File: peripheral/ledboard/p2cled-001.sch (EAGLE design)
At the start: 5 parts, among them J3 DISP, J4 PWR

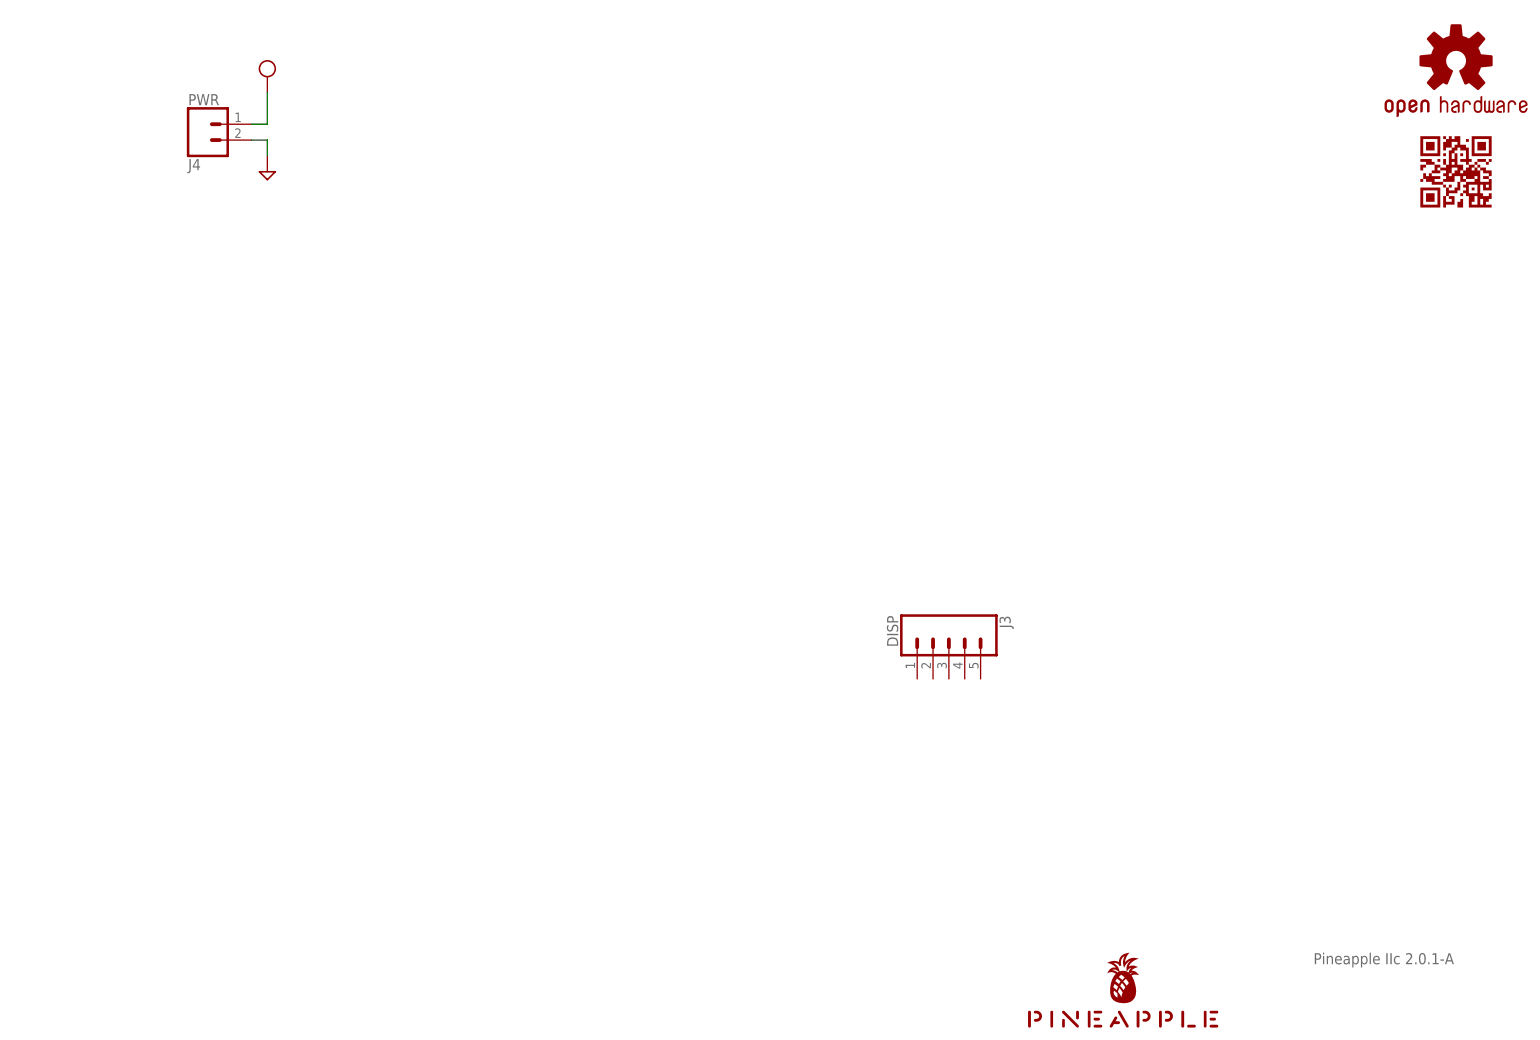
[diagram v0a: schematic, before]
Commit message: Added LED board design.
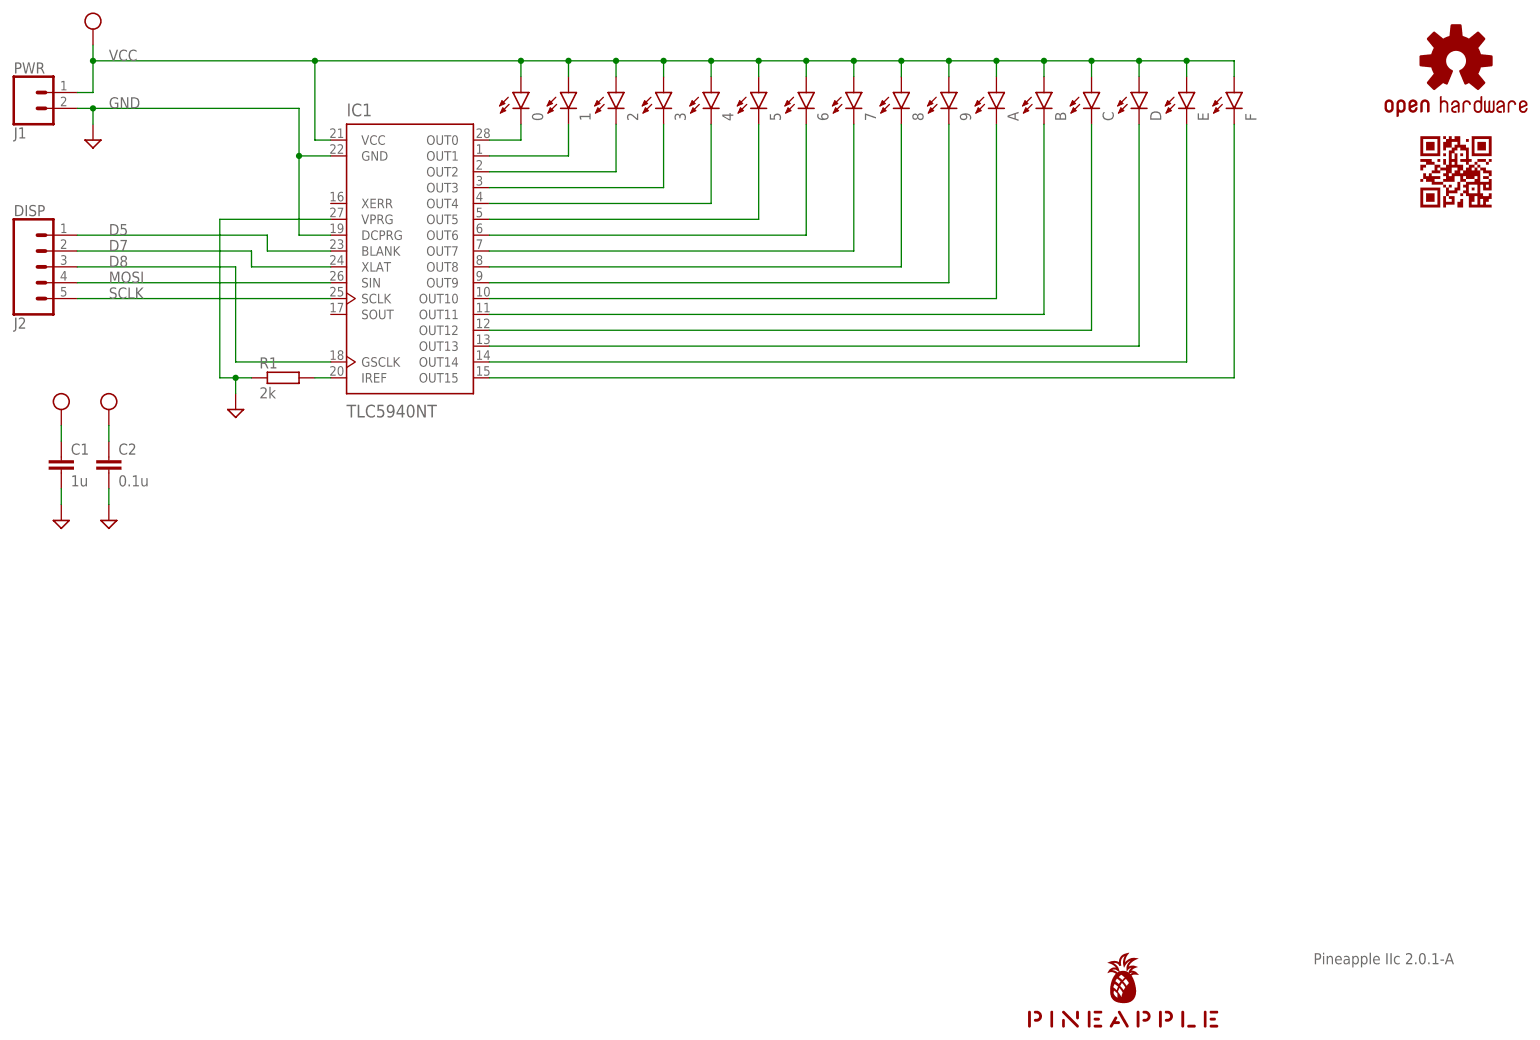
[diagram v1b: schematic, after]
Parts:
- removed J3: DISP, SparkFun-Connectors:CONN_05JST
- removed J4: PWR, SparkFun-Connectors:CONN_02JST-PTH-2
- added 0, 1, 2, 3, 4, 5, 6, 7, 8, 9, A, B, C, D, E, F: (no value), led:LEDB152
- added C1: 1u, resistor:C-EU025-024X044
- added C2: 0.1u, resistor:C-EU025-024X044
- added IC1: TLC5940NT, tlc5940:TLC5940NT
- added J1: PWR, SparkFun-Connectors:CONN_02JST-PTH-2
- added J2: DISP, SparkFun-Connectors:CONN_05JST
- added R1: 2k, resistor:R-EU_0204/5
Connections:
- new net D5: IC1.BLANK, J2.1
- new net D7: IC1.XLAT, J2.2
- new net D8: IC1.GSCLK, J2.3
- new net MOSI: IC1.SIN, J2.4
- new net N$1: 0.C, IC1.OUT0
- new net N$10: 9.C, IC1.OUT9
- new net N$11: A.C, IC1.OUT10
- new net N$12: B.C, IC1.OUT11
- new net N$13: C.C, IC1.OUT12
- new net N$14: D.C, IC1.OUT13
- new net N$15: E.C, IC1.OUT14
- new net N$16: F.C, IC1.OUT15
- new net N$17: IC1.IREF, R1.2
- new net N$2: 1.C, IC1.OUT1
- new net N$3: 2.C, IC1.OUT2
- new net N$4: 3.C, IC1.OUT3
- new net N$5: 4.C, IC1.OUT4
- new net N$6: 5.C, IC1.OUT5
- new net N$7: 6.C, IC1.OUT6
- new net N$8: 7.C, IC1.OUT7
- new net N$9: 8.C, IC1.OUT8
- new net SCLK: IC1.SCLK, J2.5
- net GND: now also C1.2, C2.2, IC1.DCPRG, IC1.GND, IC1.VPRG, J1.2, R1.1; no longer J4.2
- net VCC: now also 0.A, 1.A, 2.A, 3.A, 4.A, 5.A, 6.A, 7.A, 8.A, 9.A, A.A, B.A, C.A, C1.1, C2.1, D.A, E.A, F.A, IC1.VCC, J1.1; no longer J4.1

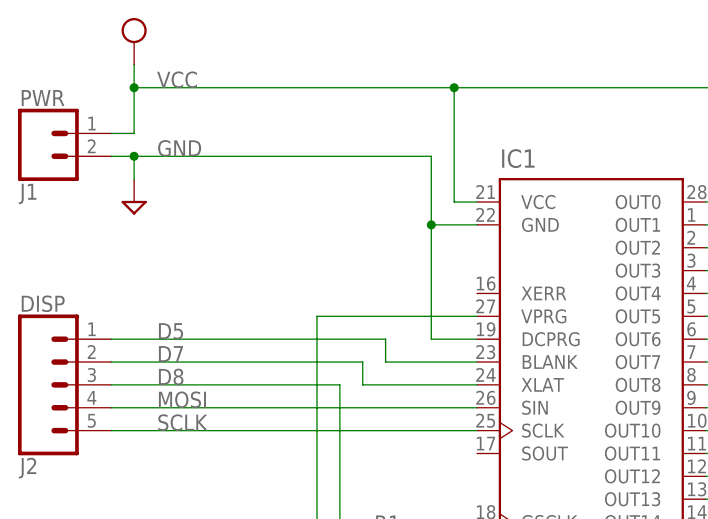
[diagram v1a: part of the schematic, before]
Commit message: Fixed connection of LED board.
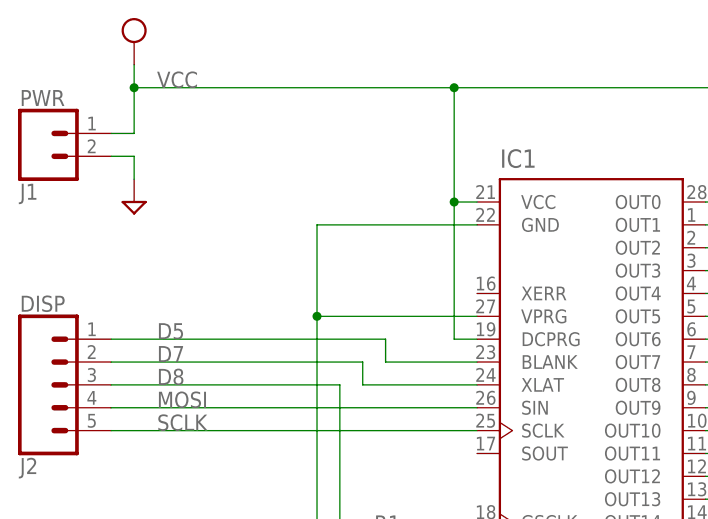
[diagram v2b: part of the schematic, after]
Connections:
- net GND: no longer IC1.DCPRG
- net VCC: now also IC1.DCPRG
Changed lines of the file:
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@@
 <net name="GND" class="1">
 <segment>
+<pinref part="SUPPLY12" gate="GND" pin="GND"/>
 <pinref part="J1" gate="G$1" pin="2"/>
 <wire x1="20.32" y1="157.48" x2="22.86" y2="157.48" width="0.1524" layer="91"/>
-<pinref part="SUPPLY12" gate="GND" pin="GND"/>
 <wire x1="22.86" y1="157.48" x2="22.86" y2="154.94" width="0.1524" layer="91"/>
-<pinref part="IC1" gate="G$1" pin="GND"/>
-<wire x1="60.96" y1="149.86" x2="55.88" y2="149.86" width="0.1524" layer="91"/>
-<wire x1="55.88" y1="149.86" x2="55.88" y2="157.48" width="0.1524" layer="91"/>
-<wire x1="55.88" y1="157.48" x2="22.86" y2="157.48" width="0.1524" layer="91"/>
-<junction x="22.86" y="157.48"/>
-<pinref part="IC1" gate="G$1" pin="DCPRG"/>
-<wire x1="60.96" y1="137.16" x2="55.88" y2="137.16" width="0.1524" layer="91"/>
-<wire x1="55.88" y1="137.16" x2="55.88" y2="149.86" width="0.1524" layer="91"/>
-<junction x="55.88" y="149.86"/>
-<label x="25.4" y="157.48" size="1.778" layer="95"/>
 </segment>
 <segment>
+<pinref part="IC1" gate="G$1" pin="GND"/>
+<wire x1="60.96" y1="149.86" x2="43.18" y2="149.86" width="0.1524" layer="91"/>
 <pinref part="R1" gate="G$1" pin="1"/>
 <wire x1="48.26" y1="114.3" x2="45.72" y2="114.3" width="0.1524" layer="91"/>
@@
 <wire x1="43.18" y1="114.3" x2="45.72" y2="114.3" width="0.1524" layer="91"/>
 <junction x="45.72" y="114.3"/>
+<wire x1="43.18" y1="149.86" x2="43.18" y2="139.7" width="0.1524" layer="91"/>
+<junction x="43.18" y="139.7"/>
 </segment>
 <segment>
@@
 <junction x="58.42" y="165.1"/>
 <label x="25.4" y="165.1" size="1.778" layer="95"/>
+<wire x1="58.42" y1="152.4" x2="58.42" y2="137.16" width="0.1524" layer="91"/>
+<junction x="58.42" y="152.4"/>
+<pinref part="IC1" gate="G$1" pin="DCPRG"/>
+<wire x1="58.42" y1="137.16" x2="60.96" y2="137.16" width="0.1524" layer="91"/>
 </segment>
 <segment>
